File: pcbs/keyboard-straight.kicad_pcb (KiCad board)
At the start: 2 copper layers, 122.9 x 112.5 mm, 42 parts

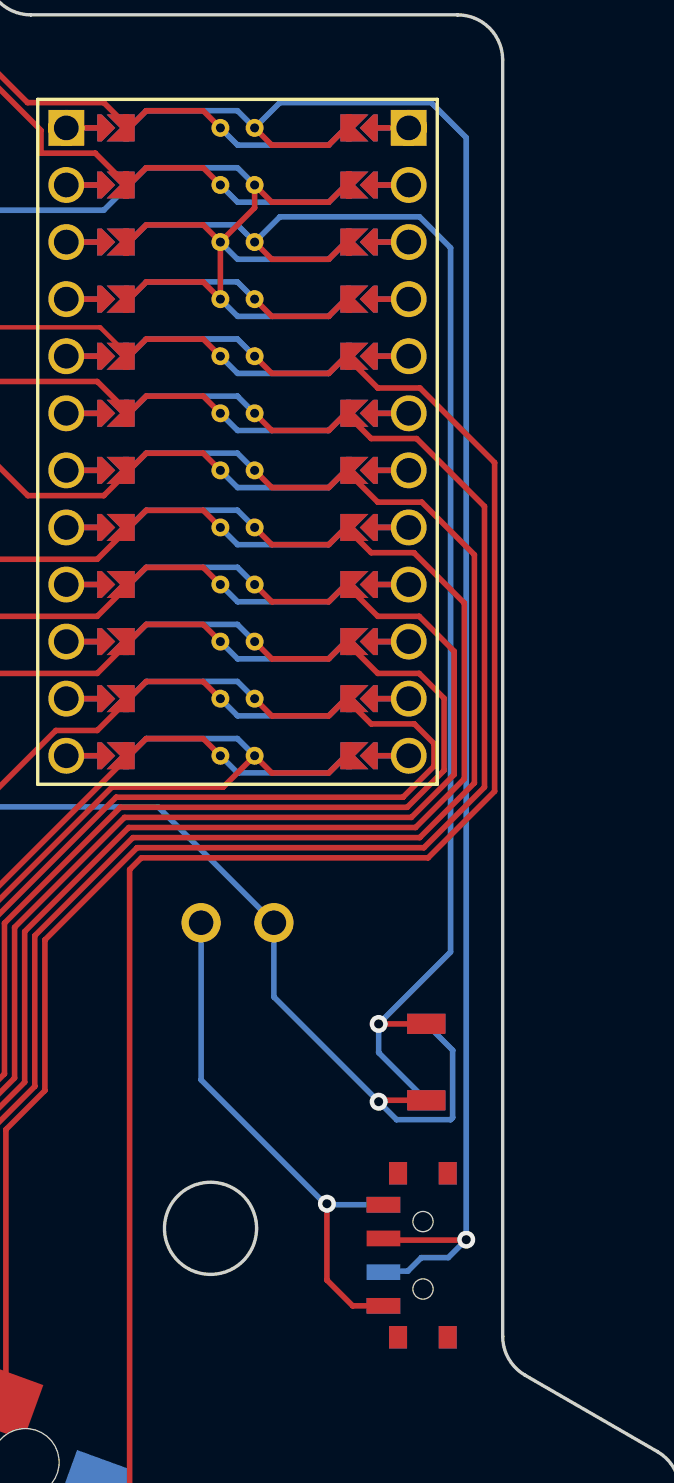
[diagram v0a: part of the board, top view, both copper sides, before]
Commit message: fixed DRC violations on straight PCB
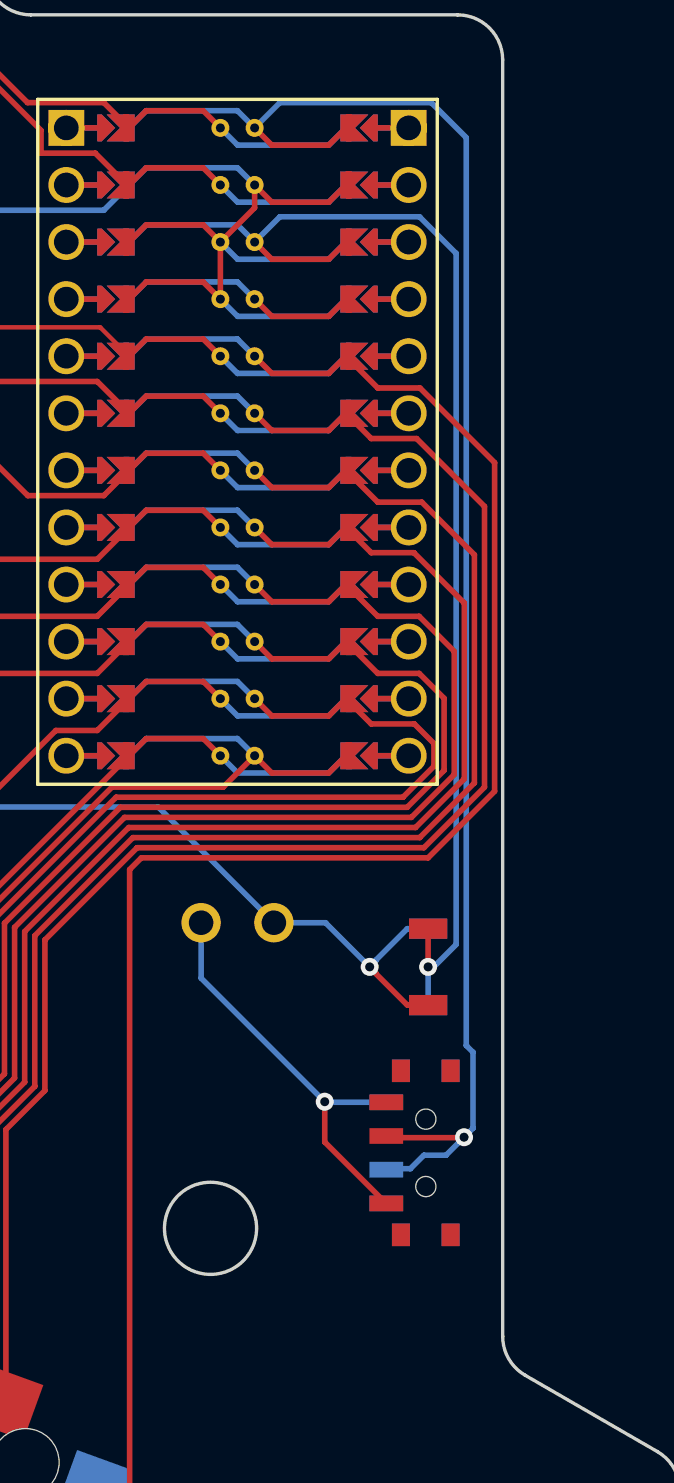
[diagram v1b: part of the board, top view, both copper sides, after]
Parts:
- moved ? 4.56 mm to (263.3, 145.1)
- moved ? 4.24 mm to (263.7, 136.9)
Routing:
- net GND: track 883.0 -> 874.3 mm
- net RST: track 52.0 -> 45.9 mm
- net pos: track 23.8 -> 18.6 mm
- net RAW: track 67.6 -> 62.9 mm
